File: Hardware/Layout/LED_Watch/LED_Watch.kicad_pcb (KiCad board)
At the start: 4 copper layers, 36 x 36 mm, 158 parts, among them IC1 MSP430FR5721, J1 CONN_01X04, SW1 SW_Push, SW2 SW_Push, Y1 Crystal

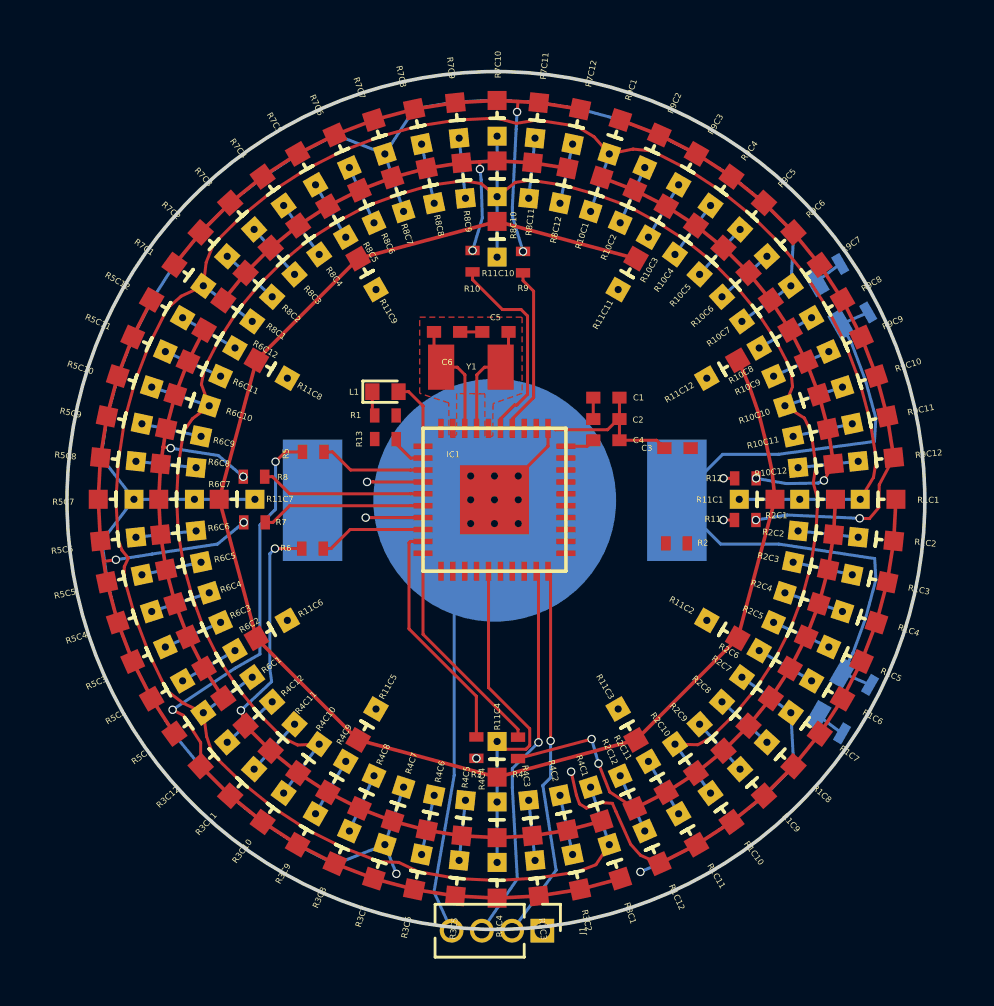
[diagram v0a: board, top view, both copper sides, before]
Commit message: Design of v1.1 complete. New features: LED light sensing capabilities. Enlarged radius of board slightly. Added "key" for 0.1" pin headers used for programming and to prevent board from rotating in enclosure. Changed all resistors and capacitors to 0402 for easier soldering
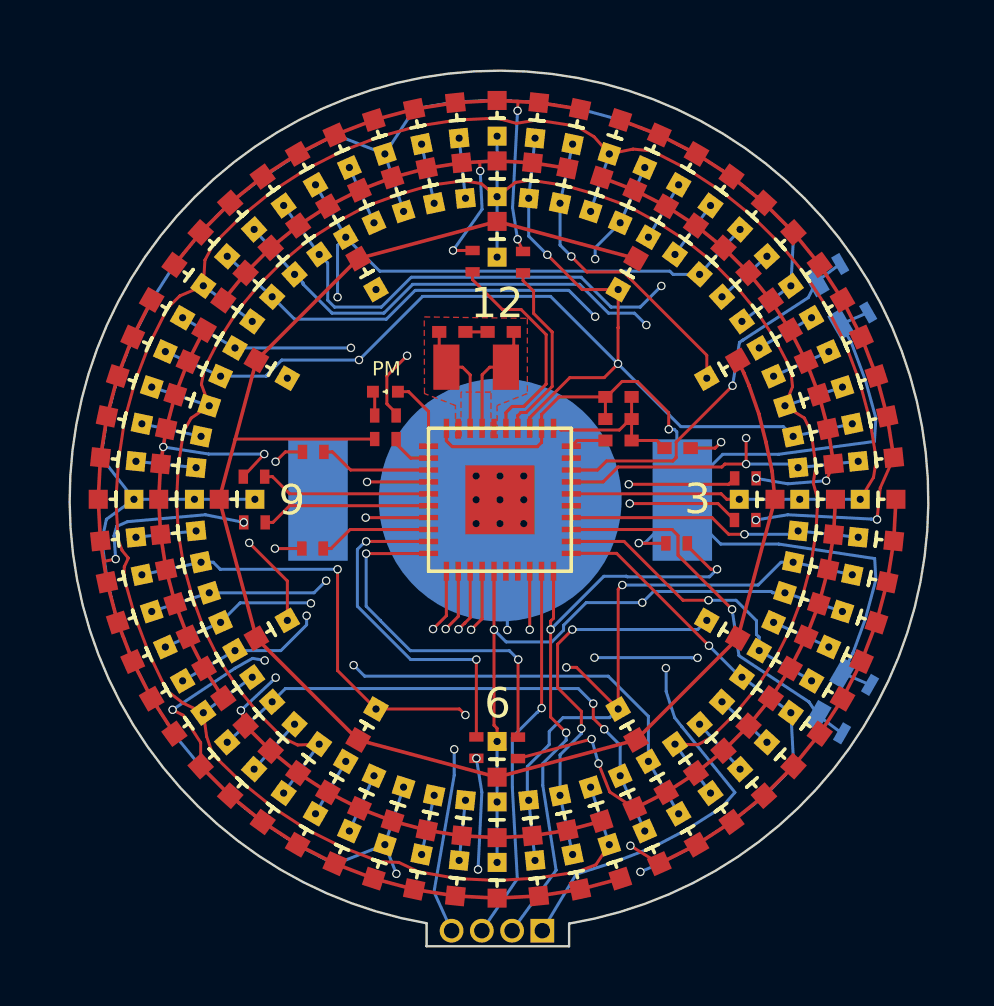
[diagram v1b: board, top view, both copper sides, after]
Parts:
- J1: footprint Pin_Headers:Pin_Header_Straight_1x04_Pitch1.27mm -> LED_Watch:Pin_Header_Straight_1x04_Pitch1.27mm
- L1: footprint LEDs:LED_0402 -> LED_Watch:LNJ247W82RA
- moved C1 0.51 mm to (103.7, 107.2)
- moved C4 0.51 mm to (103.7, 109.0)
- moved C2 0.51 mm to (103.7, 108.1)
- moved BT1 0.23 mm to (98.7, 111.5)
- moved IC1 0.23 mm to (98.7, 111.5)
- moved C5 0.22 mm to (98.7, 104.4)
- moved C6 0.22 mm to (96.7, 104.4)
- moved Y1 0.22 mm to (97.7, 105.9)
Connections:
- IC1 pad 11: /COL8 -> /COL10
- IC1 pad 12: /COL10 -> /COL5
- IC1 pad 13: Net-(IC1-Pad13) -> /COL9
- IC1 pad 14: Net-(IC1-Pad14) -> /COL8
- IC1 pad 16: /COL9 -> Net-(IC1-Pad16)
- IC1 pad 17: /COL3 -> Net-(IC1-Pad17)
- IC1 pad 18: /B2 -> /COL3
- IC1 pad 23: /COL5 -> /B2
- IC1 pad 24: Net-(IC1-Pad24) -> /COL2
- IC1 pad 25: /B1 -> Net-(IC1-Pad25)
- IC1 pad 26: /COL12 -> /COL1
- IC1 pad 27: /COL1 -> /COL12
- IC1 pad 28: /COL2 -> /B1
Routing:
- net /COL12: track 12.7 -> 93.5 mm, vias 0 -> 6
- net /COL2: track 12.7 -> 93.3 mm, vias 0 -> 6
- net /COL3: track 12.7 -> 90.0 mm, vias 0 -> 5
- net /COL11: track 12.7 -> 86.7 mm, vias 0 -> 4
- net /COL5: track 12.7 -> 83.9 mm, vias 0 -> 6
- net /COL4: track 25.1 -> 88.1 mm, vias 0 -> 4
- net +3V3: track 31.9 -> 75.8 mm, vias 0 -> 3
- net /TDO: track 15.9 -> 33.1 mm, vias 1 -> 4
- net /COL6: track 100.3 -> 117.3 mm, vias 0 -> 2
- net /COL8: track 87.7 -> 104.6 mm, vias 0 -> 1
- net /B2: track 1.25 -> 16.3 mm, vias 0 -> 1
- net /B1: track 1.25 -> 16.1 mm, vias 0 -> 1
- net /COL9: track 87.7 -> 98.0 mm, vias 0 -> 1
- net /COL10: track 84.6 -> 94.4 mm, vias 0 -> 1
- net /COL7: track 103.4 -> 113.1 mm, vias 2 -> 3
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- added copper zone on In1.Cu, net GND
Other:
- board size 36 x 36 mm -> 36.1 x 36.8 mm
- board text added: "12"
- board text added: "3"
- board text added: "6"
- board text added: "9"
- board text added: "PM"

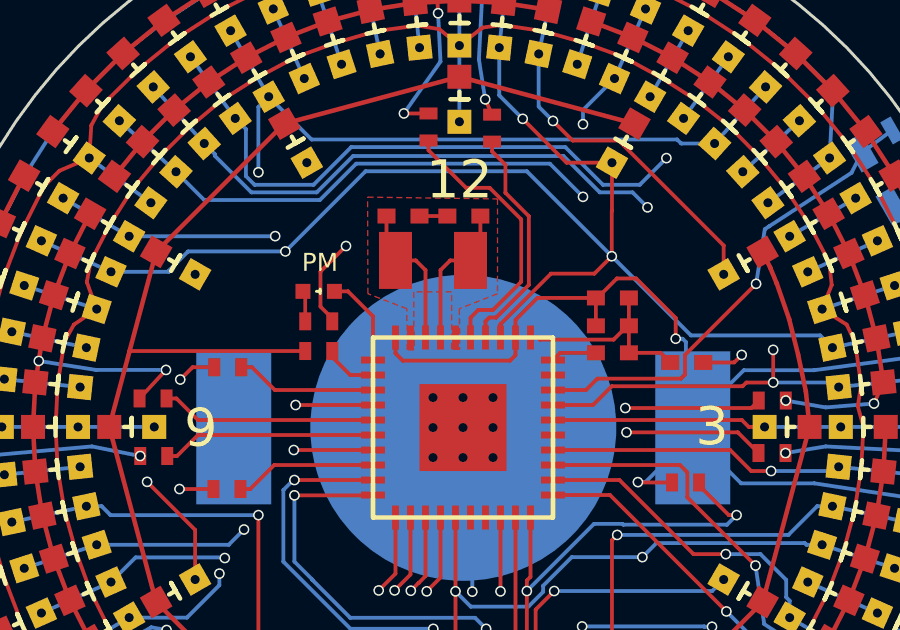
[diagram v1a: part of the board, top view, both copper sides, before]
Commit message: Fixed missing connection between osc and gnd. Fixed disconnected GNDs. Need to fix PM LED to be different LED with appropriate ratings
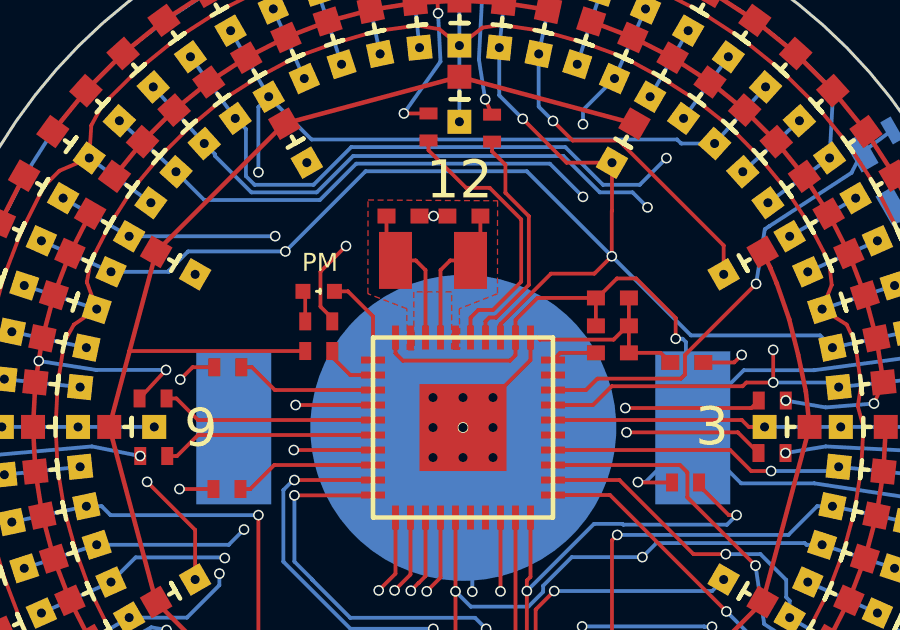
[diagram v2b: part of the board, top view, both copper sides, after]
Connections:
- C5 pad 1: Net-(C5-Pad1) -> GND
- C6 pad 1: Net-(C5-Pad1) -> GND
- IC1 pad 36: GND -> Net-(IC1-Pad36)
- IC1 pad 39: GND -> Net-(IC1-Pad36)
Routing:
- net GND: track 29.3 -> 32.8 mm, vias 3 -> 5
- net Net-(C5-Pad1): track 0.93 -> 0.00 mm
- added copper zone on F.Cu, net Net-(IC1-Pad36)
- removed copper zone on F.Cu, net GND

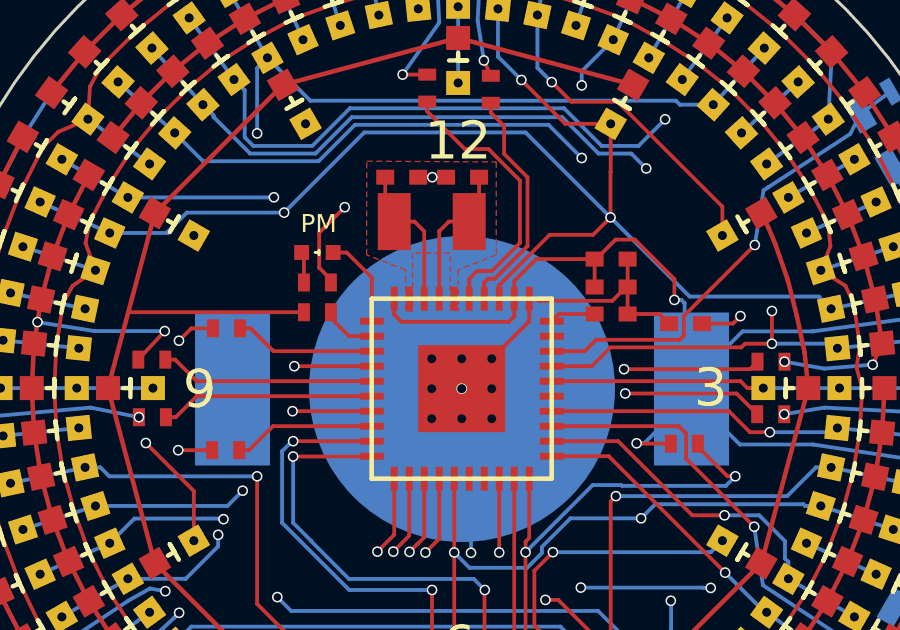
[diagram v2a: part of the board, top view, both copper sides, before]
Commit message: Changed PM LED to be the same LED package as others
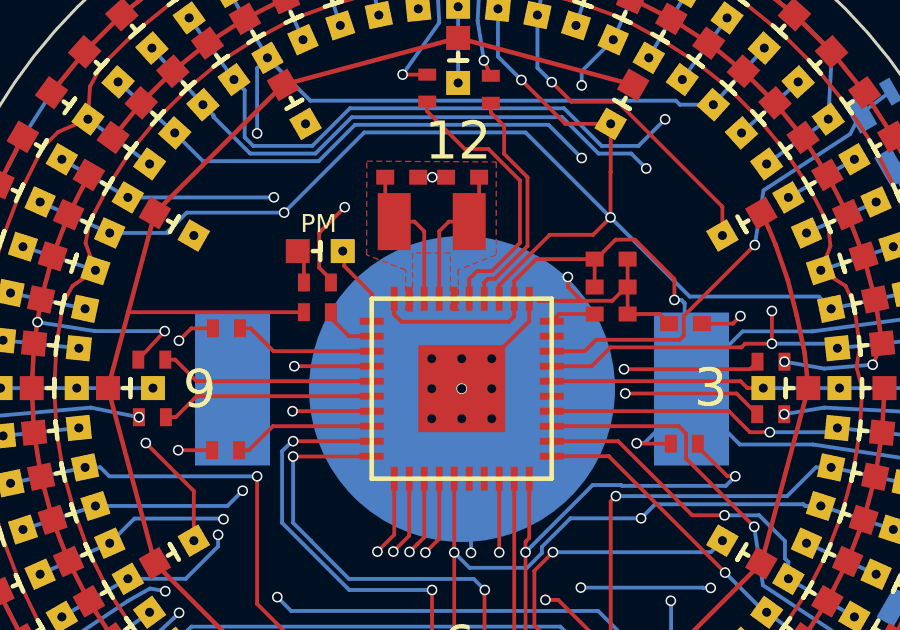
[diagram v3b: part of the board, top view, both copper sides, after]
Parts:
- L1: footprint LED_Watch:LNJ247W82RA -> LED_Watch:LSQ976
- moved L1 0.11 mm to (94.0, 106.9), turned to 180 degrees
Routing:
- net GND: track 32.8 -> 39.7 mm, vias 5 -> 6
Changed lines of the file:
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@@
     (thickness 1.6)
     (drawings 9)
-    (tracks 1146)
+    (tracks 1153)
     (zones 0)
     (modules 158)
@@
   (layers
     (0 F.Cu signal)
-    (1 In1.Cu signal)
+    (1 In1.Cu signal hide)
     (2 In2.Cu signal)
     (31 B.Cu signal)
@@
       (net 27 /COL12))
   )
-  (module LED_Watch:LNJ247W82RA (layer F.Cu)
-    (at 93.86 106.93)
-    (fp_text reference L1 (at -1.15 0.004) (layer Dwgs.User)
-      (effects (font (size 0.25 0.25) (thickness 0.0625)))
-    )
-    (fp_text value LED (at 0 -1.5) (layer F.Fab)
-      (effects (font (size 1 1) (thickness 0.15)))
-    )
-    (fp_line (start 0.05 0) (end -0.075 0) (layer F.SilkS) (width 0.1))
-    (fp_line (start 0.05 -0.075) (end 0.05 0.075) (layer F.SilkS) (width 0.1))
-    (pad 2 smd rect (at 0.525 0) (size 0.5 0.5) (layers F.Cu F.Paste F.Mask)
-      (net 33 /PM_LED))
-    (pad 1 smd rect (at -0.525 0) (size 0.5 0.5) (layers F.Cu F.Paste F.Mask)
-      (net 34 "Net-(L1-Pad1)"))
-  )
   (module LED_Watch:Pin_Header_Straight_1x04_Pitch1.27mm (layer F.Cu)
     (at 100.45 129.57 270)
@@
     )
   )
+  (module LED_Watch:LSQ976 (layer F.Cu)
+    (at 93.9546 106.8832 180)
+    (fp_text reference L1 (at 1.524 0 180) (layer Dwgs.User)
+      (effects (font (size 0.254 0.254) (thickness 0.0635)))
+    )
+    (fp_text value LED (at 0.75 -0.6 180) (layer F.Fab)
+      (effects (font (size 0.254 0.254) (thickness 0.0635)))
+    )
+    (fp_line (start 0 -0.3) (end 0 0.3) (layer F.SilkS) (width 0.15))
+    (fp_line (start 0 0.3) (end 0 0) (layer F.SilkS) (width 0.15))
+    (fp_line (start 0 0) (end 0.25 0) (layer F.SilkS) (width 0.15))
+    (pad 1 smd rect (at 0.75 0 180) (size 0.8 0.8) (layers F.Cu F.Paste F.Mask)
+      (net 34 "Net-(L1-Pad1)"))
+    (pad 2 thru_hole rect (at -0.75 0 180) (size 0.8 0.8) (drill 0.3) (layers *.Cu *.Mask)
+      (net 33 /PM_LED))
+  )
+  (gr_arc (start 98.63 111.48) (end 101.574924 129.271925) (angle -340.8898998) (layer Edge.Cuts) (width 0.1))
   (gr_text PM (at 93.9 105.97) (layer F.SilkS)
     (effects (font (size 0.6 0.6) (thickness 0.1)))
@@
   (gr_line (start 95.587833 130.223185) (end 101.574924 130.223185) (layer Edge.Cuts) (width 0.1))
   (gr_line (start 95.587833 129.255556) (end 95.587833 130.223185) (layer Edge.Cuts) (width 0.1))
-  (gr_arc (start 98.63 111.48) (end 101.574924 129.271925) (angle -340.8898998) (layer Edge.Cuts) (width 0.1))
   (gr_text 9 (at 89.93 111.49) (layer F.SilkS)
     (effects (font (size 1.2714 1.2714) (thickness 0.254)))
@@
     (effects (font (size 1.2714 1.2714) (thickness 0.254)))
   )
+  (segment (start 102.2096 107.7468) (end 98.68 111.2764) (width 0.127) (layer B.Cu) (net 1))
+  (segment (start 98.68 111.2764) (end 98.68 111.48) (width 0.127) (layer B.Cu) (net 1))
+  (segment (start 101.9556 108.539499) (end 103.690501 108.539499) (width 0.127) (layer F.Cu) (net 1))
+  (segment (start 101.231499 108.539499) (end 101.9556 108.539499) (width 0.127) (layer F.Cu) (net 1))
+  (segment (start 102.666597 108.539499) (end 102.2096 108.082502) (width 0.127) (layer F.Cu) (net 1))
+  (segment (start 102.2096 108.082502) (end 102.2096 107.7468) (width 0.127) (layer F.Cu) (net 1))
+  (segment (start 101.9556 108.539499) (end 102.666597 108.539499) (width 0.127) (layer F.Cu) (net 1))
+  (via (at 102.2096 107.7468) (size 0.3556) (drill 0.254) (layers F.Cu B.Cu) (net 1))
   (via (at 97.6884 104.42) (size 0.3556) (drill 0.254) (layers F.Cu B.Cu) (net 1))
   (via (at 98.67 111.47) (size 0.3556) (drill 0.254) (layers F.Cu B.Cu) (net 1))
@@
   (segment (start 100.92 108.47) (end 101.162 108.47) (width 0.127) (layer F.Cu) (net 1) (status 10))
   (segment (start 101.162 108.47) (end 101.231499 108.539499) (width 0.127) (layer F.Cu) (net 1))
-  (segment (start 101.231499 108.539499) (end 103.690501 108.539499) (width 0.127) (layer F.Cu) (net 1))
   (segment (start 103.690501 108.539499) (end 104.15 108.08) (width 0.127) (layer F.Cu) (net 1) (status 20))
   (segment (start 104.15 108.08) (end 104.2 108.08) (width 0.127) (layer F.Cu) (net 1) (status 30))
@@
   (segment (start 86.210874 102.4851) (end 88.265777 103.978074) (width 0.127) (layer B.Cu) (net 32) (status 30))
   (segment (start 86.210874 120.4149) (end 88.265777 118.921926) (width 0.127) (layer B.Cu) (net 32) (status 30))
-  (segment (start 94.385 106.93) (end 94.837 106.93) (width 0.127) (layer F.Cu) (net 33))
-  (segment (start 95.67 107.763) (end 95.67 109.22) (width 0.127) (layer F.Cu) (net 33) (status 20))
-  (segment (start 94.837 106.93) (end 95.67 107.763) (width 0.127) (layer F.Cu) (net 33))
-  (segment (start 93.41 107.93) (end 93.41 107.005) (width 0.127) (layer F.Cu) (net 34))
-  (segment (start 93.41 107.005) (end 93.335 106.93) (width 0.127) (layer F.Cu) (net 34))
+  (segment (start 95.67 109.22) (end 95.67 108.2994) (width 0.127) (layer F.Cu) (net 33))
+  (segment (start 95.67 108.2994) (end 94.7554 107.3848) (width 0.127) (layer F.Cu) (net 33))
+  (segment (start 94.7554 107.3848) (end 94.7554 106.8578) (width 0.127) (layer F.Cu) (net 33))
+  (segment (start 93.41 107.93) (end 93.41 107.0124) (width 0.127) (layer F.Cu) (net 34))
+  (segment (start 93.41 107.0124) (end 93.2554 106.8578) (width 0.127) (layer F.Cu) (net 34))
   (segment (start 93.31 107.83) (end 93.41 107.93) (width 0.127) (layer F.Cu) (net 34) (status 30))
   (segment (start 104.15 126) (end 105.363651 126.753713) (width 0.127) (layer F.Cu) (net 35))

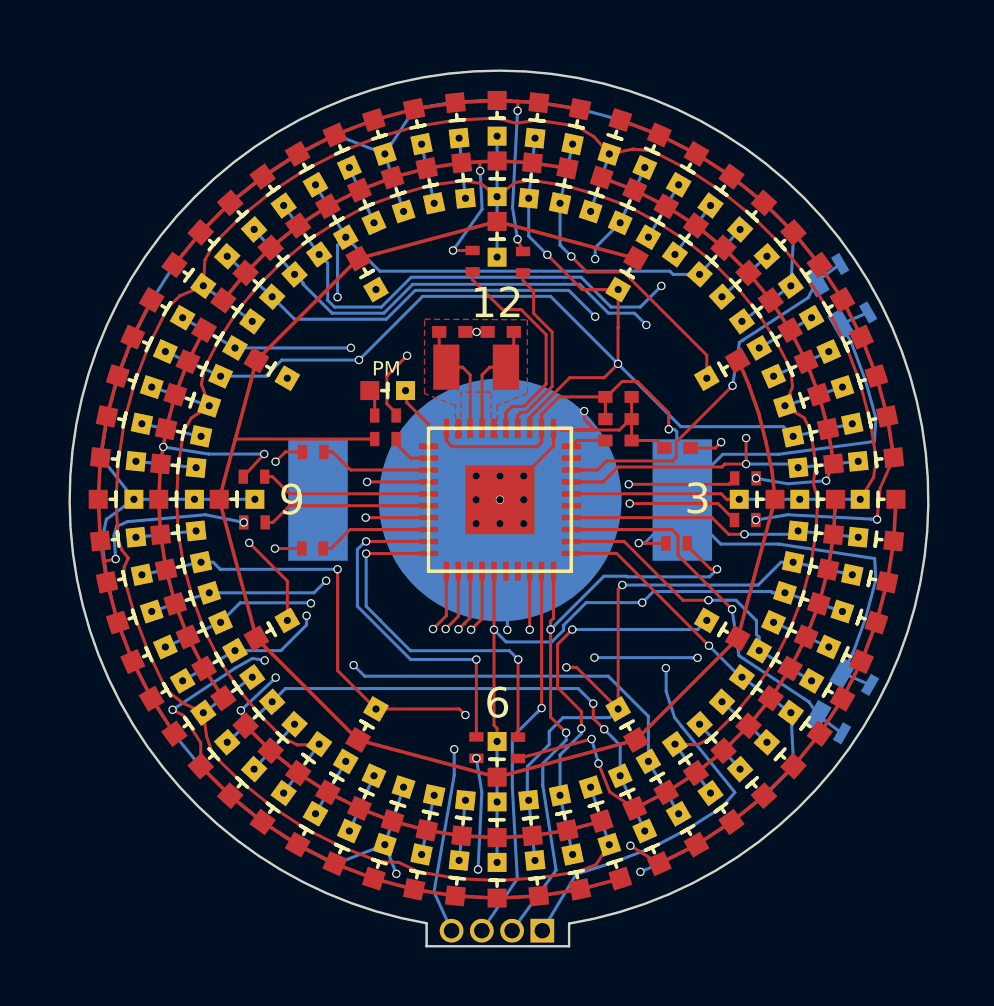
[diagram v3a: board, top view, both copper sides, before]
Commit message: Moved debug headers to an offset angle due to watch housing interference.
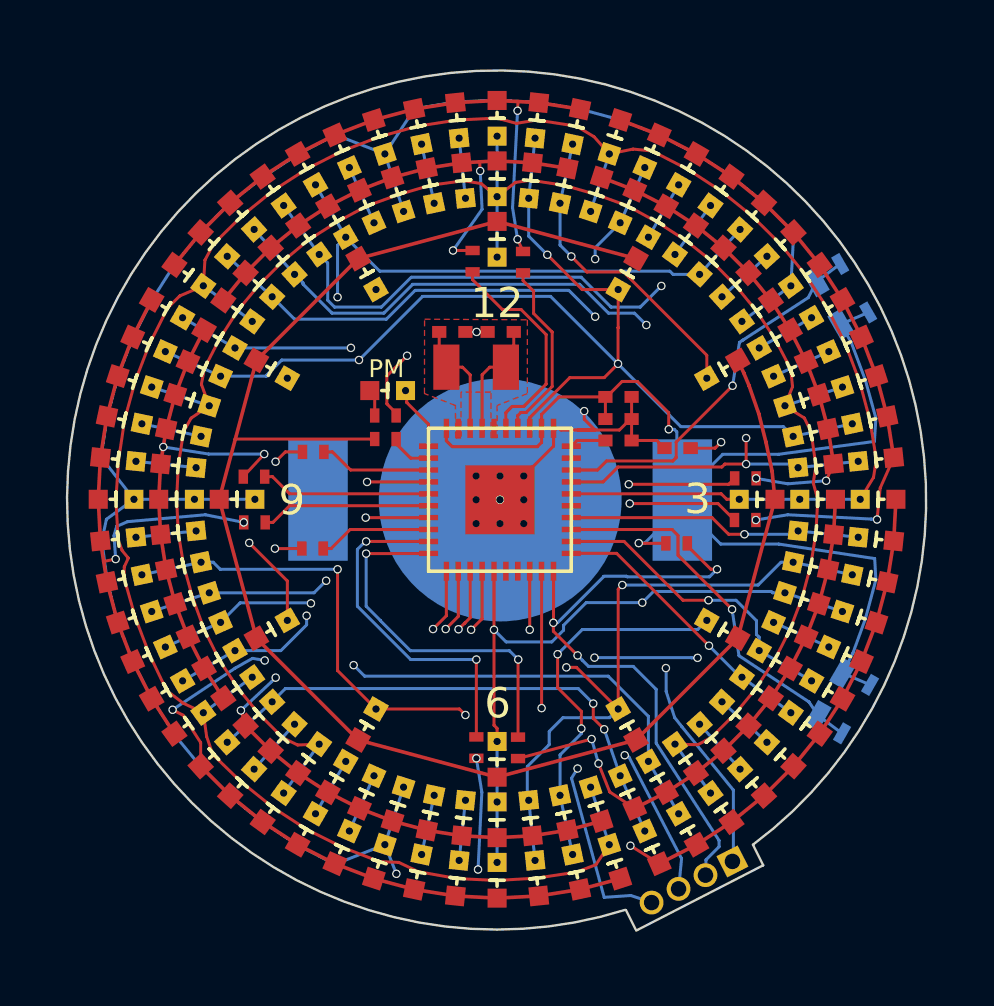
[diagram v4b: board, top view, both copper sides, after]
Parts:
- moved J1 8.50 mm to (108.4, 126.7), turned to 297 degrees
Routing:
- net GND: track 39.7 -> 28.4 mm, vias 6 -> 5
- net +3V3: track 75.8 -> 68.5 mm
- net /COL2: track 93.3 -> 94.4 mm
- net /TCK: track 16.1 -> 16.7 mm, vias 1 -> 2
- net /COL7: vias 3 -> 2
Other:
- board size 36.1 x 36.8 mm -> 36.1 x 36.1 mm
